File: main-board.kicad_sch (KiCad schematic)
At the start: 0 parts

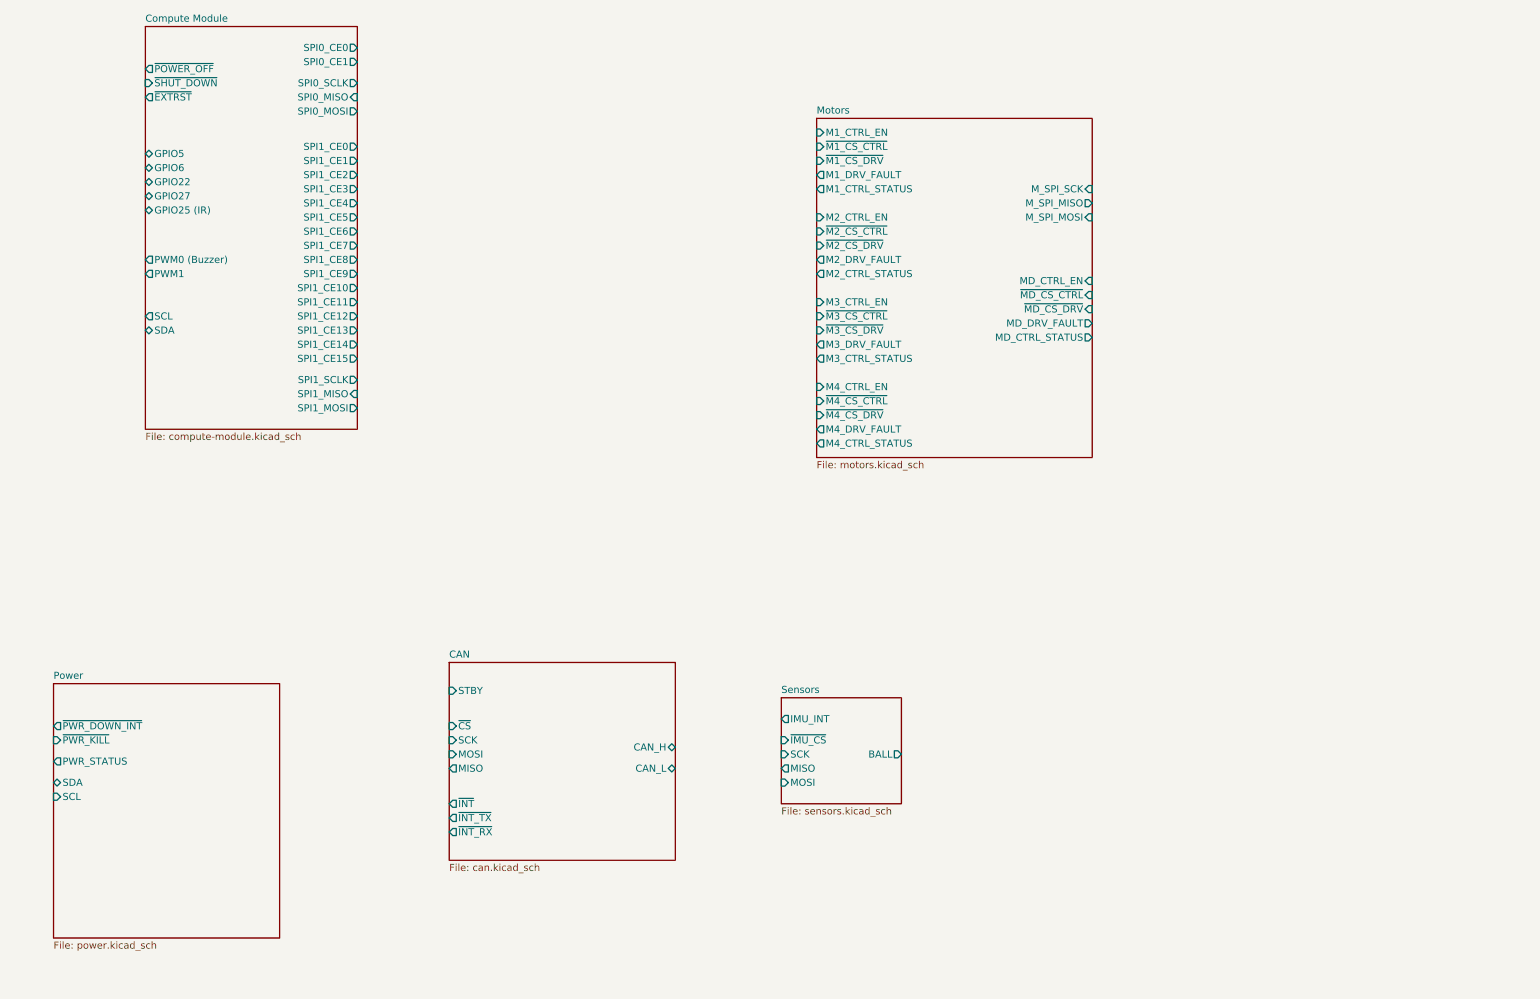
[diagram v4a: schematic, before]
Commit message: Add RP2040
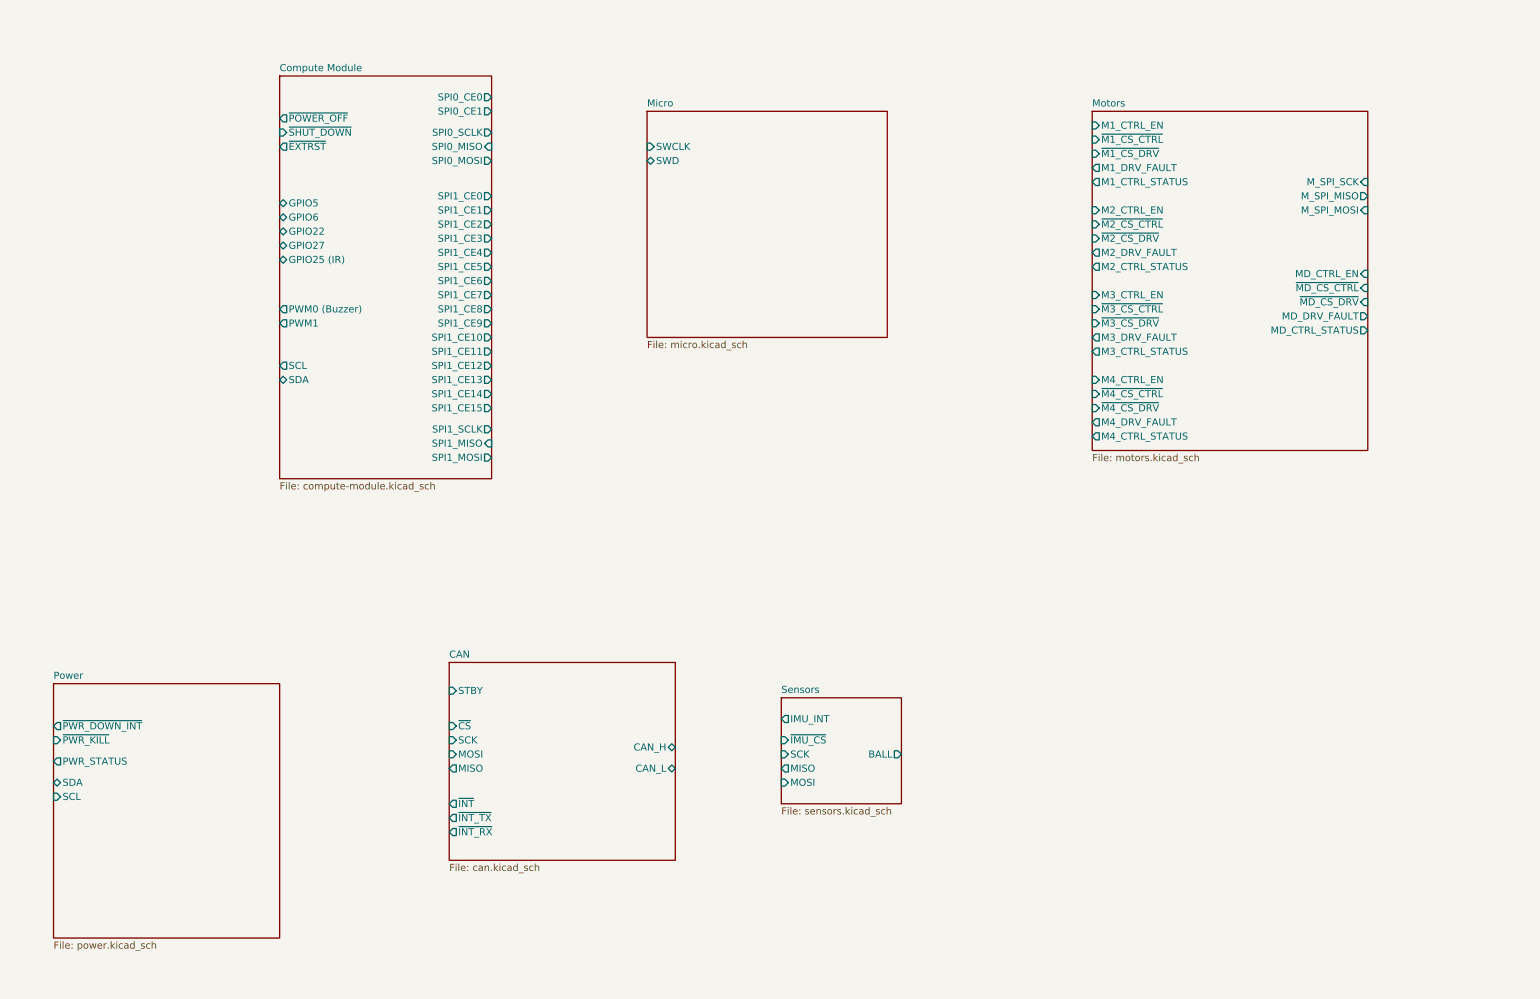
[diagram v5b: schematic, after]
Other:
- added sheet Micro (micro.kicad_sch)

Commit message: Finish RP2040 connections.
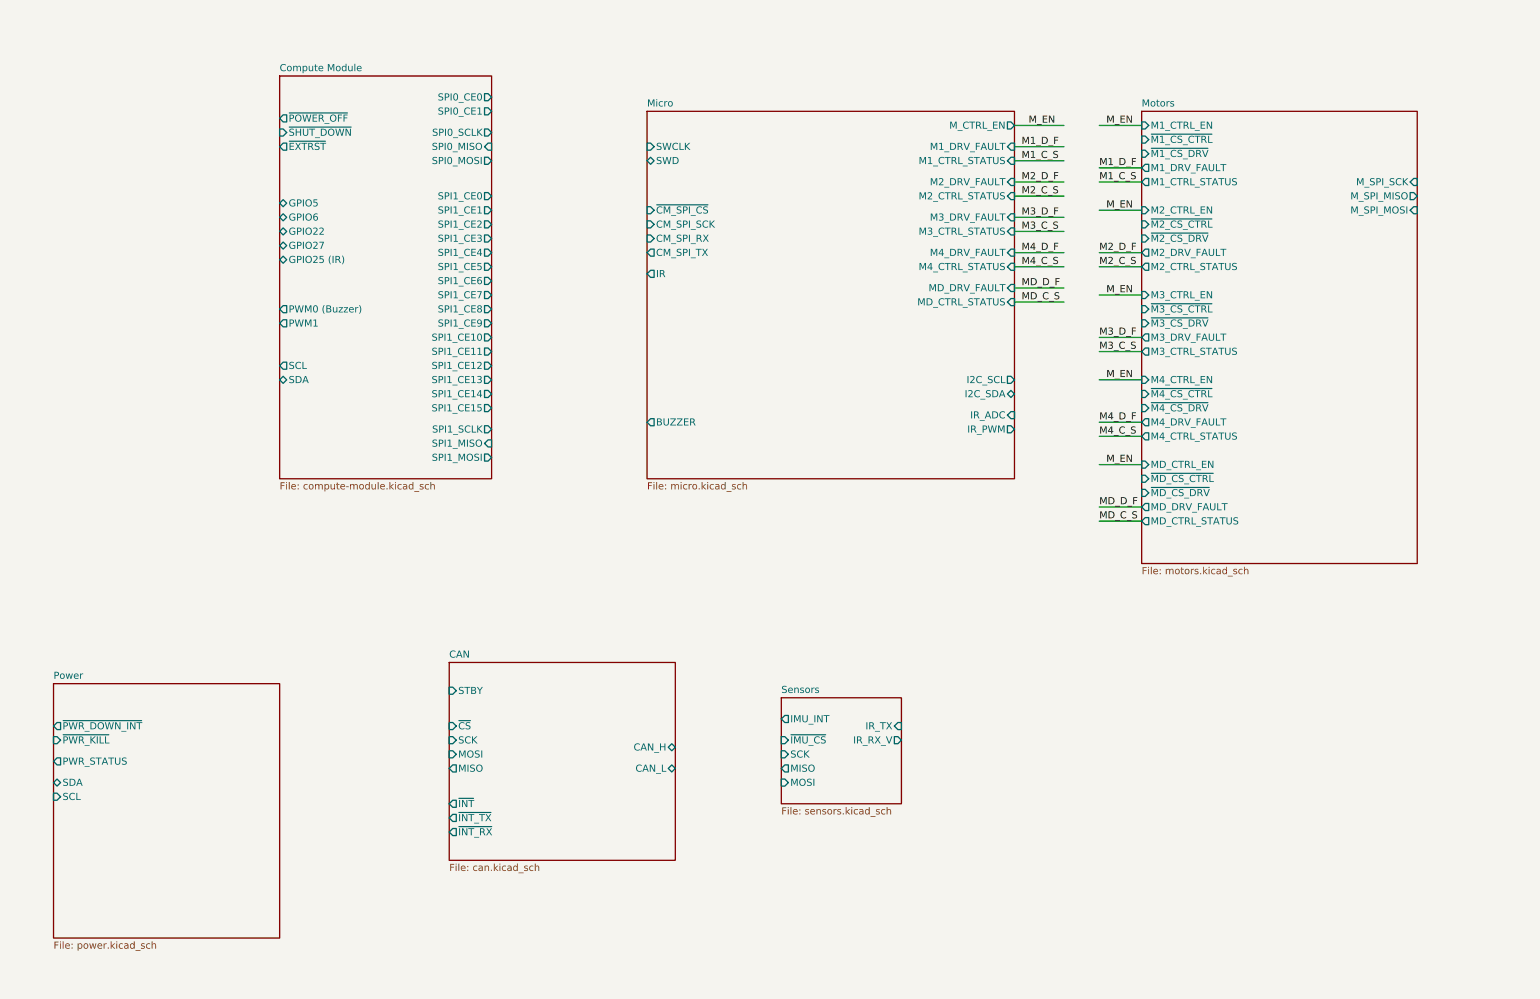
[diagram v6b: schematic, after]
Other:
- sheet Micro ports: added BUZZER, CM_SPI_RX, CM_SPI_SCK, CM_SPI_TX, I2C_SCL, I2C_SDA, IR, IR_ADC, IR_PWM, M1_CTRL_STATUS, M1_DRV_FAULT, M2_CTRL_STATUS, M2_DRV_FAULT, M3_CTRL_STATUS, M3_DRV_FAULT, M4_CTRL_STATUS, M4_DRV_FAULT, MD_CTRL_STATUS, MD_DRV_FAULT, M_CTRL_EN, ~{CM_SPI_CS}; removed none
- sheet Sensors ports: added IR_RX_V, IR_TX; removed BALL

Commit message: Finish connecting everything in sch.
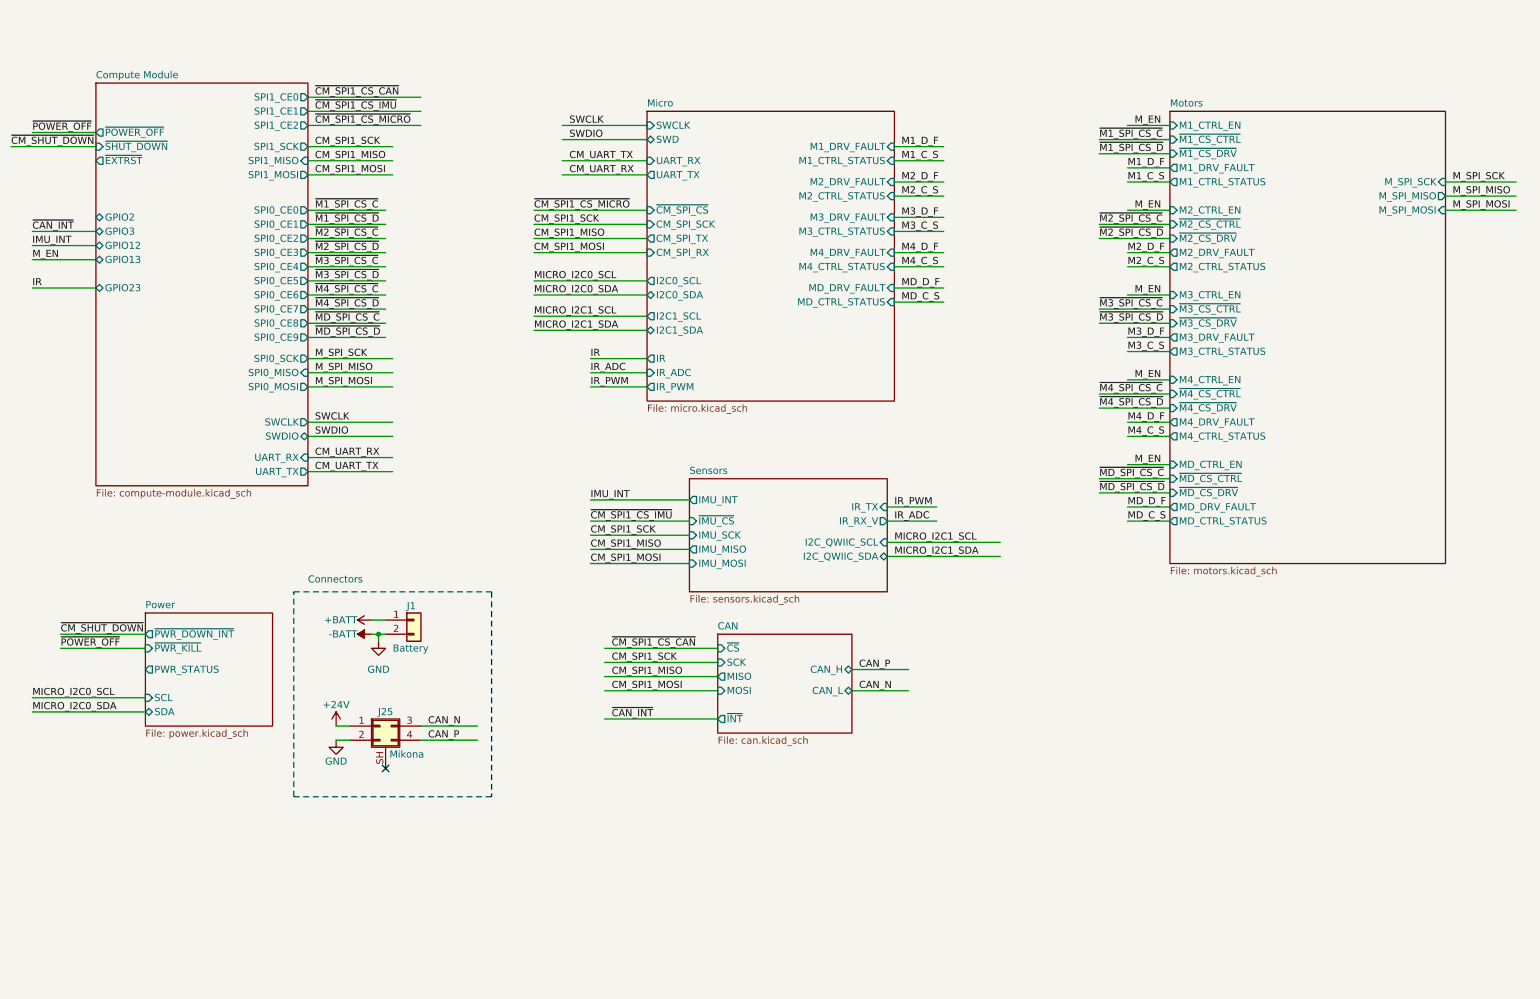
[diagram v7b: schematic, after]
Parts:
- added J1: Battery, Connector_AMASS:AMASS_XT60PW-M_1x02_P7.20mm_Horizontal, symbol Connector_Generic:Conn_01x02
- added J25: Mikona, 1054291104:MOLEX_1054291104, symbol Connector_Generic_Shielded:Conn_02x02_Top_Bottom_Shielded
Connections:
- new net +24V: J25.1 (Pin_1)
- new net +BATT: J1.1 (Pin_1)
- new net -BATT: J1.2 (Pin_2), J25.2 (Pin_2)
- new net CAN_N: J25.3 (Pin_3)
- new net CAN_P: J25.4 (Pin_4)
- no-connect marks 0 -> 1
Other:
- sheet CAN ports: added none; removed STBY, ~{INT_RX}, ~{INT_TX}
- sheet Compute Module ports: added GPIO12, GPIO13, GPIO2, GPIO23, GPIO3, SPI0_CE2, SPI0_CE3, SPI0_CE4, SPI0_CE5, SPI0_CE6, SPI0_CE7, SPI0_CE8, SPI0_CE9, SPI0_SCK, SPI1_SCK, SWCLK, SWDIO, UART_RX, UART_TX; removed GPIO22, GPIO25 (IR), GPIO27, GPIO5, GPIO6, PWM0 (Buzzer), PWM1, SCL, SDA, SPI0_SCLK, SPI1_CE10, SPI1_CE11, SPI1_CE12, SPI1_CE13, SPI1_CE14, SPI1_CE15, SPI1_CE3, SPI1_CE4, SPI1_CE5, SPI1_CE6, SPI1_CE7, SPI1_CE8, SPI1_CE9, SPI1_SCLK
- sheet Micro ports: added I2C0_SCL, I2C0_SDA, I2C1_SCL, I2C1_SDA, UART_RX, UART_TX; removed BUZZER, I2C_SCL, I2C_SDA, M_CTRL_EN
- sheet Sensors ports: added I2C_QWIIC_SCL, I2C_QWIIC_SDA, IMU_MISO, IMU_MOSI, IMU_SCK; removed MISO, MOSI, SCK
- note added: "Connectors"

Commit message: Fix sch errors and warnings.
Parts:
- added R17: 2mΩ, symbol Device:R_Small_US
- J1: MPN (none) -> XT60PW-M
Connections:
- net +24V: now also R17.2; no longer J25.1 (Pin_1)
- net -BATT renamed GND
- new net SENSE_MIKONA: J25.1 (Pin_1), R17.1
- no-connect marks 1 -> 4
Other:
- sheet Power ports: added SENSE_MIKONA; removed none
- moved on the sheet: J1, J25
